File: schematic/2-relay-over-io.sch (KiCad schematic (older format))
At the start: 25 parts, among them J1 Conn_02x08_Odd_Even, J2 Conn_02x08_Odd_Even, Q2 BC817, Q3 BC817, U1 SONGLE_3V_relay, U2 SONGLE_3V_relay, U6 DizzyBITLogo, U7 DizzyBIT-Layout

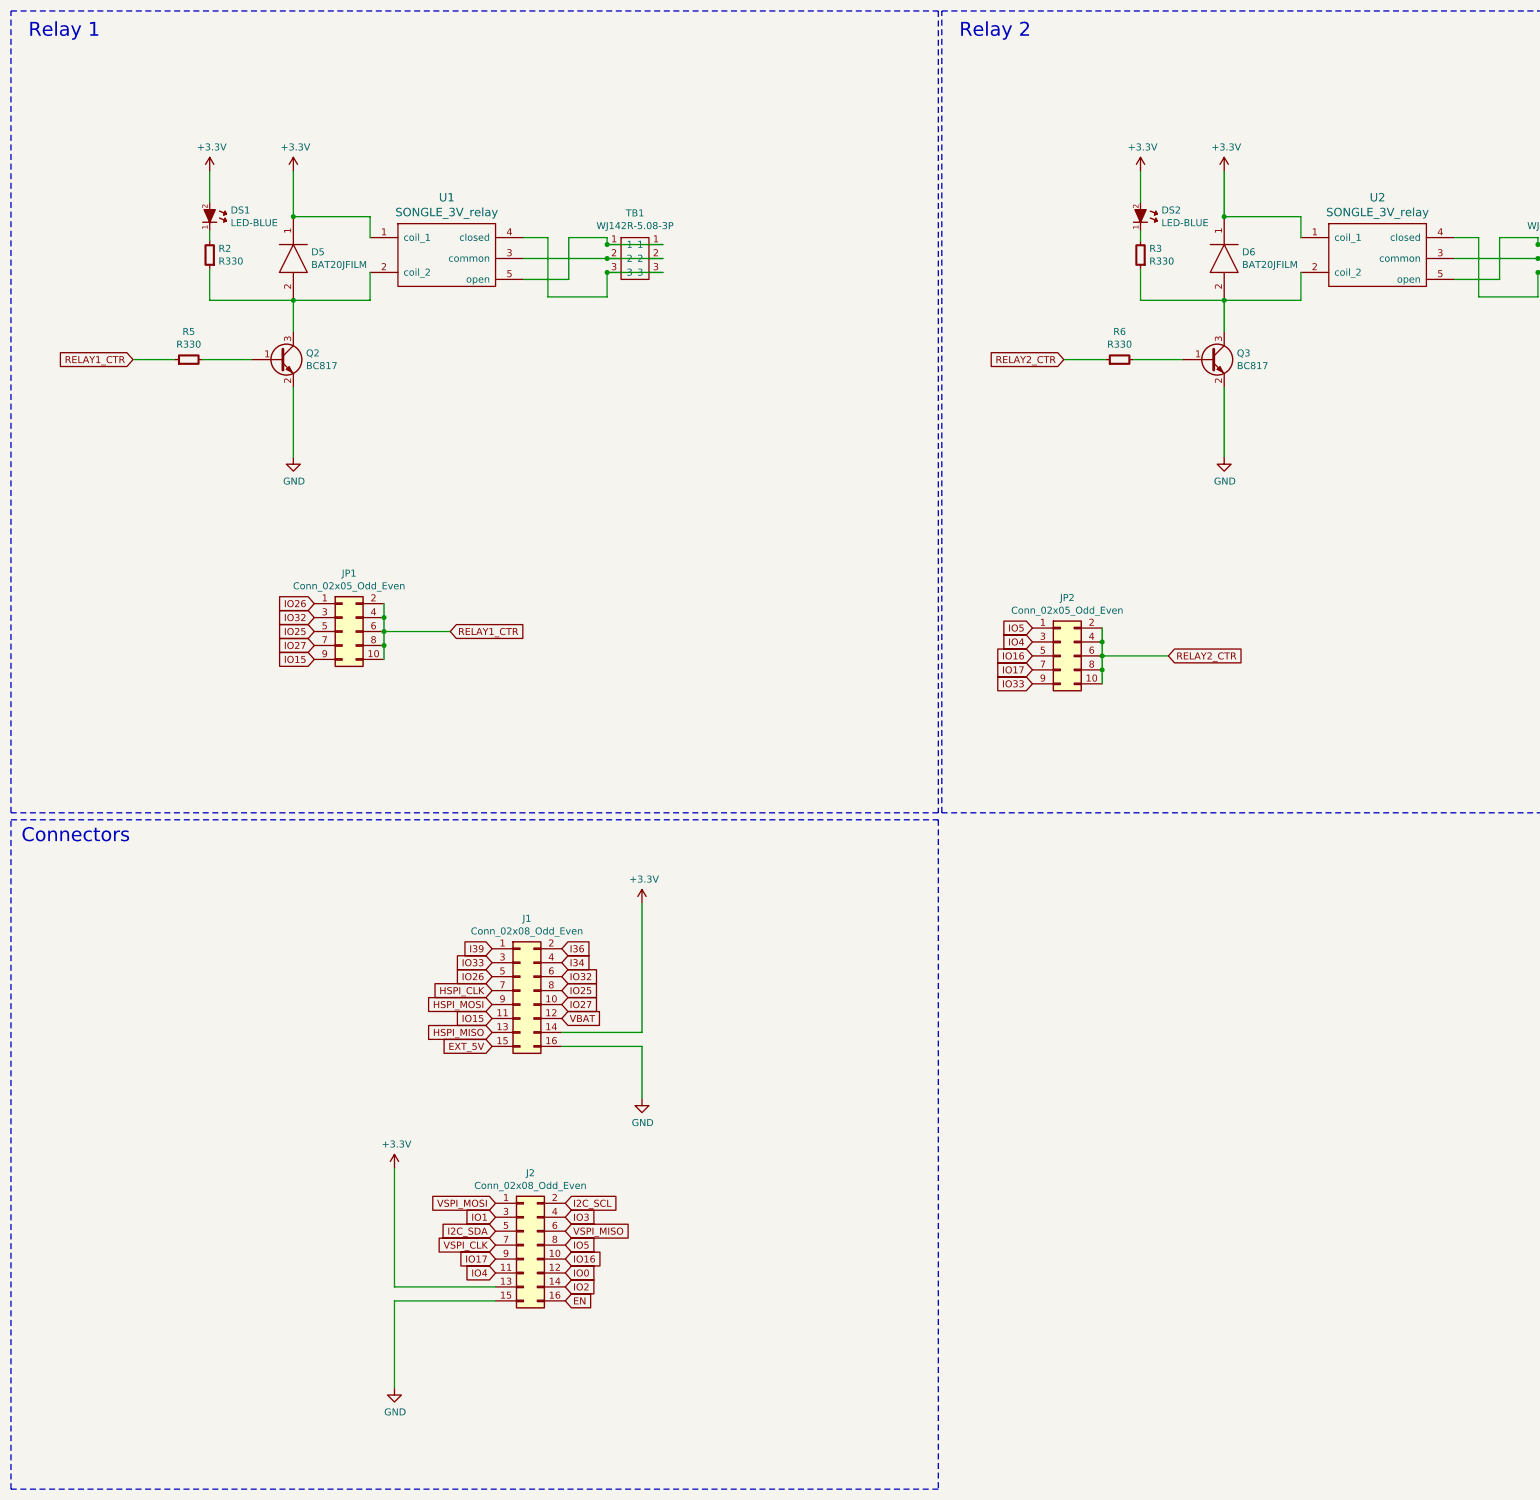
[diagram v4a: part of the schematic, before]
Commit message: Major Update. Changed pin configuration and board outline. Relays now use the 5V load in order to avoid stressing the regulator.
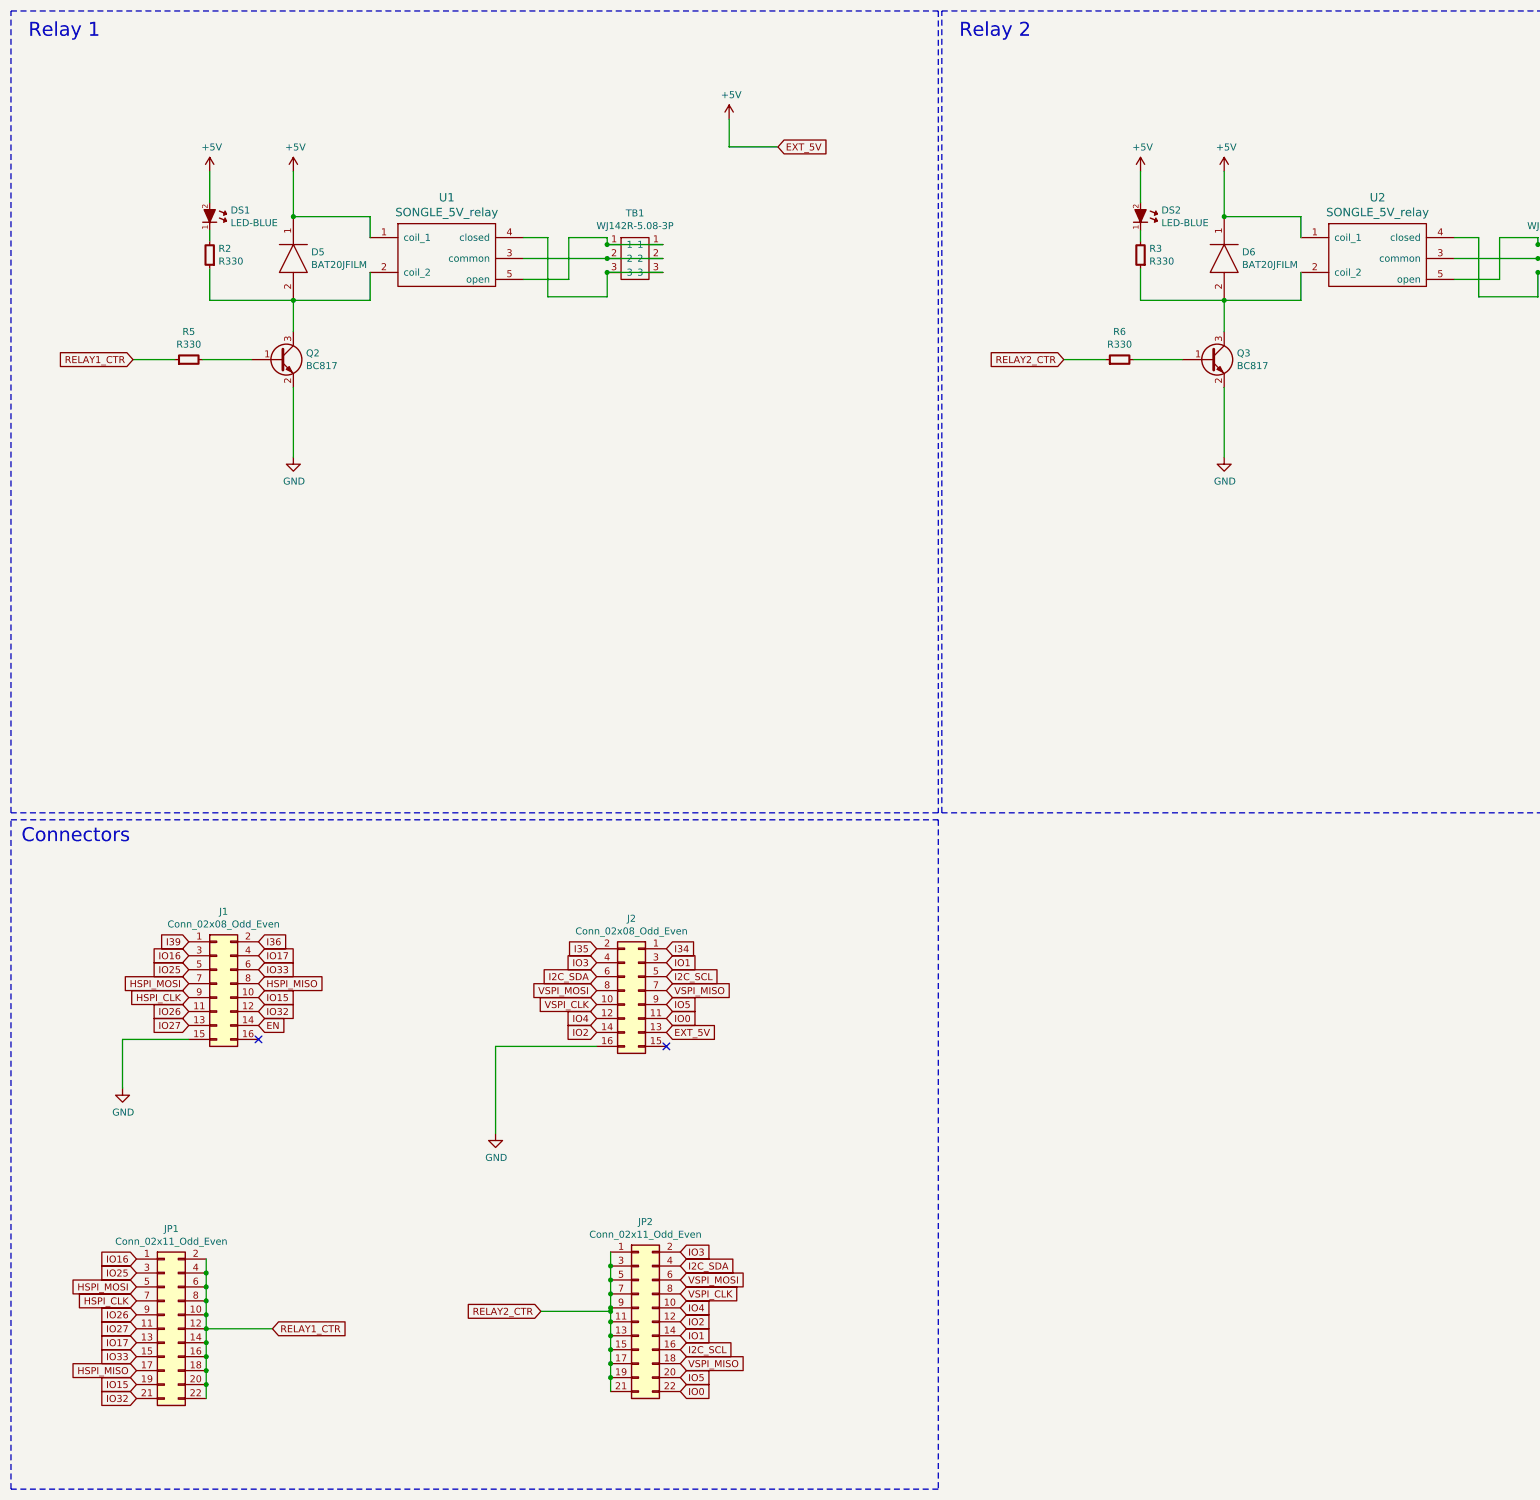
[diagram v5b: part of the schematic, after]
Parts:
- removed JP1, JP2: Conn_02x05_Odd_Even, DizzyBit:DizzyBit-SolderJumper-5-5-Open, symbol Connector_Generic:Conn_02x05_Odd_Even
- added JP1, JP2: Conn_02x11_Odd_Even, Connector_PinHeader_2.00mm:PinHeader_2x11_P2.00mm_Vertical, symbol Connector_Generic:Conn_02x11_Odd_Even
- J1, J2: footprint Connector_PinHeader_2.54mm:PinHeader_2x08_P2.54mm_Vertical -> Connector_PinSocket_2.54mm:PinSocket_2x08_P2.54mm_Vertical; pn PC104-003-2*8-B-1 -> PC104-013-2*8-B-1
- U1, U2: value SONGLE_3V_relay -> SONGLE_5V_relay; footprint Songle:SONGLE_3V_Relay -> Songle:SONGLE_5V_Relay; pn SRD-03VDC-SL-C -> SRD-05VDC-SL-C
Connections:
- net EXT_5V is gone; now on net GND: J1.15 (Pin_15)
- net VBAT is gone; now on net IO32: J1.12 (Pin_12)
- net EN: now also J1.14 (Pin_14); no longer J2.16 (Pin_16)
- net GND: now also J2.16 (Pin_16); no longer J1.16 (Pin_16), J2.15 (Pin_15)
- net HSPI_CLK: now also J1.9 (Pin_9), JP1.7 (Pin_7); no longer J1.7 (Pin_7)
- net HSPI_MISO: now also J1.8 (Pin_8), JP1.17 (Pin_17); no longer J1.13 (Pin_13)
- net HSPI_MOSI: now also J1.7 (Pin_7), JP1.5 (Pin_5); no longer J1.9 (Pin_9)
- net I2C_SCL: now also J2.5 (Pin_5), JP2.16 (Pin_16); no longer J2.2 (Pin_2)
- net I2C_SDA: now also J2.6 (Pin_6), JP2.4 (Pin_4); no longer J2.5 (Pin_5)
- net I34: now also J2.1 (Pin_1); no longer J1.4 (Pin_4)
- net IO0: now also J2.11 (Pin_11), JP2.22 (Pin_22); no longer J2.12 (Pin_12)
- net IO1: now also JP2.14 (Pin_14)
- net IO15: now also J1.10 (Pin_10), JP1.19 (Pin_19); no longer J1.11 (Pin_11)
- net IO16: now also J1.3 (Pin_3), JP1.1 (Pin_1); no longer J2.10 (Pin_10)
- net IO17: now also J1.4 (Pin_4), JP1.13 (Pin_13); no longer J2.9 (Pin_9)
- net IO2: now also JP2.12 (Pin_12)
- net IO25: now also J1.5 (Pin_5), JP1.3 (Pin_3); no longer J1.8 (Pin_8)
- net IO26: now also J1.11 (Pin_11), JP1.9 (Pin_9); no longer J1.5 (Pin_5)
- net IO27: now also J1.13 (Pin_13), JP1.11 (Pin_11); no longer J1.10 (Pin_10)
- net IO3: now also JP2.2 (Pin_2)
- net IO32: now also JP1.21 (Pin_21); no longer J1.6 (Pin_6)
- net IO33: now also J1.6 (Pin_6), JP1.15 (Pin_15); no longer J1.3 (Pin_3)
- net IO4: now also J2.12 (Pin_12), JP2.10 (Pin_10); no longer J2.11 (Pin_11)
- net IO5: now also J2.9 (Pin_9), JP2.20 (Pin_20); no longer J2.8 (Pin_8)
- net RELAY1_CTR: now also JP1.10 (Pin_10), JP1.12 (Pin_12), JP1.14 (Pin_14), JP1.16 (Pin_16), JP1.18 (Pin_18), JP1.2 (Pin_2), JP1.20 (Pin_20), JP1.22 (Pin_22), JP1.4 (Pin_4), JP1.6 (Pin_6), JP1.8 (Pin_8)
- net RELAY2_CTR: now also JP2.1 (Pin_1), JP2.11 (Pin_11), JP2.13 (Pin_13), JP2.15 (Pin_15), JP2.17 (Pin_17), JP2.19 (Pin_19), JP2.21 (Pin_21), JP2.3 (Pin_3), JP2.5 (Pin_5), JP2.7 (Pin_7), JP2.9 (Pin_9)
- net VSPI_CLK: now also J2.10 (Pin_10), JP2.8 (Pin_8); no longer J2.7 (Pin_7)
- net VSPI_MISO: now also J2.7 (Pin_7), JP2.18 (Pin_18); no longer J2.6 (Pin_6)
- net VSPI_MOSI: now also J2.8 (Pin_8), JP2.6 (Pin_6); no longer J2.1 (Pin_1)
- net +3V3 renamed +5V
- net +5V: no longer J1.14 (Pin_14)
- new net I35: J2.2 (Pin_2)
- no-connect marks 0 -> 2
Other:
- moved on the sheet: J1, J2
